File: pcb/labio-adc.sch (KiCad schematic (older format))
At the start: 14 parts, among them P301 CONN_01X04, P302 CONN_01X04, P303 CONN_01X04, Q301 PHOTOTRANSISTOR, Q302 Q_NMOS_GSD, Q303 Q_NMOS_GSD, SW301 DIP_SWITCH_X04, U301 ADS1015

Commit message: finish rerouting for new parts
* fix adc power supply nets
* redo adc layout
* move motor controller up to make space for headers
* add motor controller heatsink mount
* fix motor controller ground pad net

todo:
* silkscreen
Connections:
- net VDD_J is gone; now on net VDD5V_J: R301.1
- net SCL_5V: now reaches Q302.3 (D), R303.2, U301.10 (SCL)
- net SDA_5V: now reaches Q303.3 (D), R304.2, U301.9 (SDA)
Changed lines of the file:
@@
 $Descr A4 11693 8268
 encoding utf-8
-Sheet 3 9
+Sheet 3 10
 Title ""
 Date ""
@@
 INT_J
 Text Label 5100 4600 0    60   ~ 0
-VDD_J
+VDD5V_J
 $Comp
 L Q_NMOS_GSD Q303
@@
 Text Notes 7100 6000 0    60   ~ 0
 5V <=> 3.3V level shifting
+Text Label 7000 4700 0    60   ~ 0
+SDA_5V
+Text Label 7000 5400 0    60   ~ 0
+SCL_5V
 $EndSCHEMATC

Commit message: add bom. change led resistors to 220 and dnp rpi hat eeprom
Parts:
- R302: value 2k -> 220
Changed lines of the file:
@@
 P 8100 3800
 F 0 "R302" H 8130 3820 50  0000 L CNN
-F 1 "2k" H 8130 3760 50  0000 L CNN
+F 1 "220" H 8130 3760 50  0000 L CNN
 F 2 "Resistors_SMD:R_0603" H 8100 3800 50  0001 C CNN
 F 3 "" H 8100 3800 50  0000 C CNN

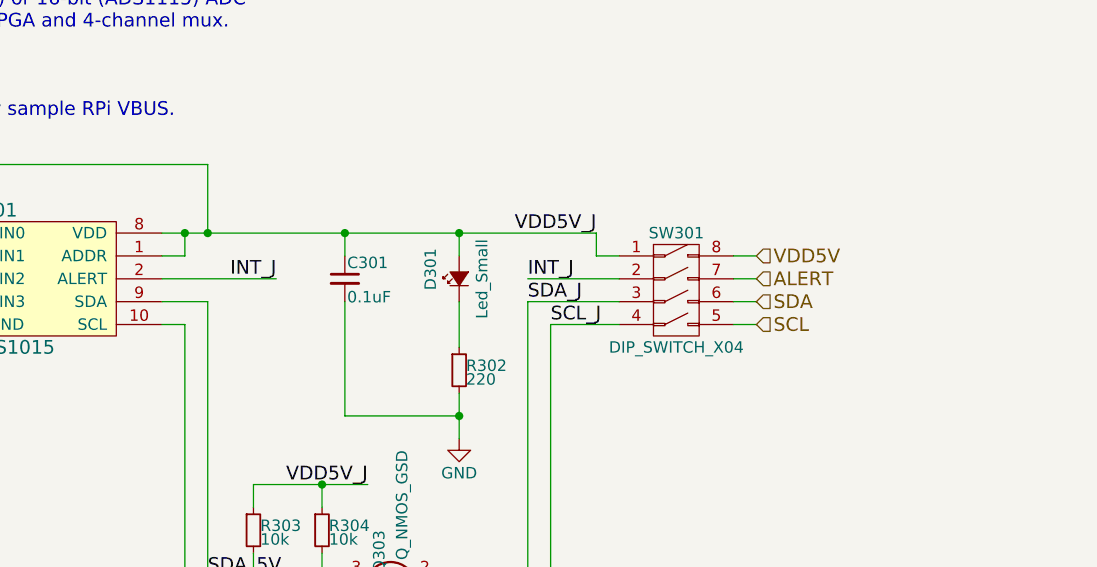
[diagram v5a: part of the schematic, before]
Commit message: add fuses for connectable headers (adc, encoder, motors, servo, codec). GERBER/BOM UPDATES ONLY
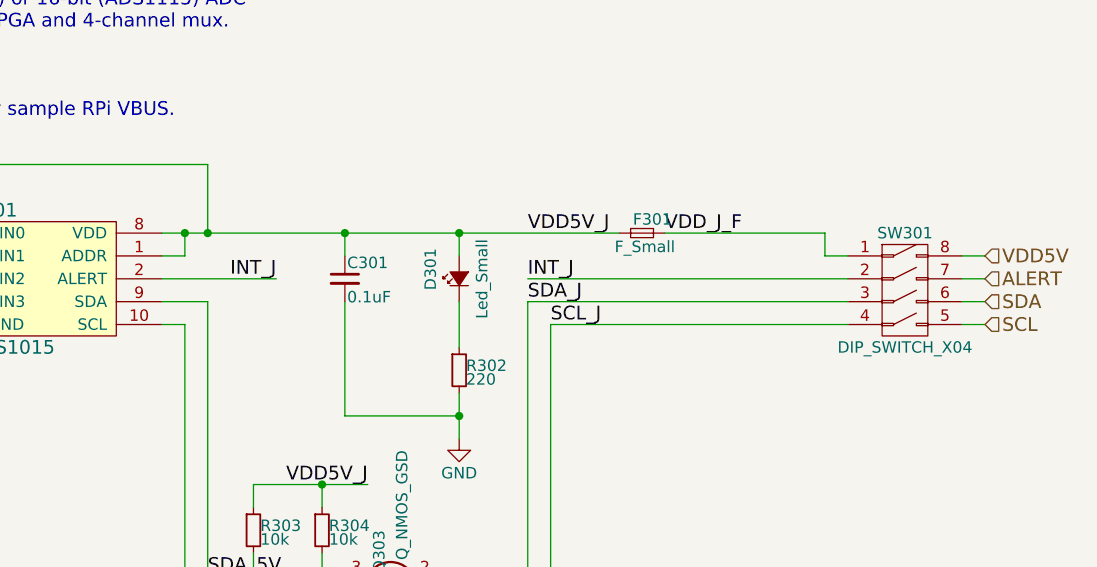
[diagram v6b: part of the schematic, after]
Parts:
- added F301: F_Small, Resistors_SMD:R_1206, symbol F_Small
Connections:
- net VDD5V_J: now also F301.1; no longer SW301.1 (1A)
- new net VDD_J_F: F301.2, SW301.1 (1A)
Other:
- moved on the sheet: SW301
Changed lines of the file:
@@
 	1    0    0    -1
 $EndComp
-Text HLabel 9400 3300 2    60   Input ~ 0
+Text HLabel 10400 3300 2    60   Input ~ 0
 VDD5V
-Text HLabel 9400 3500 2    60   Input ~ 0
+Text HLabel 10400 3500 2    60   Input ~ 0
 SDA
-Text HLabel 9400 3600 2    60   Input ~ 0
+Text HLabel 10400 3600 2    60   Input ~ 0
 SCL
-Text HLabel 9400 3400 2    60   Input ~ 0
+Text HLabel 10400 3400 2    60   Input ~ 0
 ALERT
 Wire Wire Line
@@
 L DIP_SWITCH_X04 SW301
 U 1 1 576D562D
-P 9050 3450
-F 0 "SW301" H 9050 3700 50  0000 C CNN
-F 1 "DIP_SWITCH_X04" H 9050 3200 50  0000 C CNN
-F 2 "labio-special:DIP-8_W7.62mm_SMT" H 9050 2250 50  0001 C CNN
-F 3 "" H 9050 2250 50  0000 C CNN
-	1    9050 3450
+P 10050 3450
+F 0 "SW301" H 10050 3700 50  0000 C CNN
+F 1 "DIP_SWITCH_X04" H 10050 3200 50  0000 C CNN
+F 2 "labio-special:DIP-8_W7.62mm_SMT" H 10050 2250 50  0001 C CNN
+F 3 "" H 10050 2250 50  0000 C CNN
+	1    10050 3450
 	1    0    0    -1
 $EndComp
@@
 	8100 3500 8100 3700
 Wire Wire Line
-	8800 3400 8400 3400
-Wire Wire Line
-	8400 3500 8800 3500
-Wire Wire Line
-	8800 3600 8500 3600
-Wire Wire Line
-	8800 3300 8700 3300
-Wire Wire Line
-	8700 3300 8700 3200
-Wire Wire Line
-	8700 3200 6800 3200
+	9800 3400 8400 3400
+Wire Wire Line
+	8400 3500 9800 3500
+Wire Wire Line
+	9800 3600 8500 3600
+Wire Wire Line
+	6800 3200 8800 3200
 Wire Wire Line
 	6900 3300 6900 3200
@@
 Connection ~ 8100 3200
 Wire Wire Line
-	9400 3300 9300 3300
-Wire Wire Line
-	9300 3400 9400 3400
-Wire Wire Line
-	9400 3500 9300 3500
-Wire Wire Line
-	9300 3600 9400 3600
-Text Label 8700 3200 2    60   ~ 0
+	10400 3300 10300 3300
+Wire Wire Line
+	10300 3400 10400 3400
+Wire Wire Line
+	10400 3500 10300 3500
+Wire Wire Line
+	10300 3600 10400 3600
+Text Label 8400 3200 0    60   ~ 0
 VDD5V_J
 Text Label 8400 3400 0    60   ~ 0
@@
 Text Label 7000 5400 0    60   ~ 0
 SCL_5V
+$Comp
+L F_Small F301
+U 1 1 57A54096
+P 8900 3200
+F 0 "F301" H 8860 3260 50  0000 L CNN
+F 1 "F_Small" H 8780 3140 50  0000 L CNN
+F 2 "Resistors_SMD:R_1206" H 8900 3200 50  0001 C CNN
+F 3 "" H 8900 3200 50  0000 C CNN
+	1    8900 3200
+	1    0    0    -1
+$EndComp
+Wire Wire Line
+	9000 3200 9700 3200
+Wire Wire Line
+	9700 3200 9700 3300
+Wire Wire Line
+	9700 3300 9800 3300
+Text Label 9000 3200 0    60   ~ 0
+VDD_J_F
 $EndSCHEMATC

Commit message: Fix ADC reading mic, possible backpowering, encoder pull downs, vias in footprint:
* Mic needs on-board path to ADC. Add proper bias and amp. Connect to ADC or codec with switches.
* Mic footprint (U701) flipped. Redraw footprint and adjust routing.
* Remove power from dip switches and replace with fuses. Turning power off to a block could result in backpower from driven IO lines.
* Remove/adjust pull downs on LEDs for encoder/dpad lines.
* Move vias out of display connector (P401) footprint.
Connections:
- net ADC_AIN2: now also SW301.1 (1A)
- net VDD5V: now also F301.2; no longer SW301.8 (1B)
- net ACD_AIN0 renamed ADC_AIN0
- removed net VDD_J_F: F301.2, SW301.1 (1A)
- new net MEMS_MIC_TO_ADC: SW301.8 (1B)
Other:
- moved on the sheet: F301, SW301
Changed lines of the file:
@@
 encoding utf-8
 Sheet 3 10
-Title ""
+Title "Raspberry Pi Embedded Lab I/O"
 Date ""
-Rev ""
-Comp ""
+Rev "1.1.4"
+Comp "Carnegie Mellon University"
 Comment1 ""
-Comment2 ""
+Comment2 "Drawn by: Ian Hartwig"
 Comment3 ""
 Comment4 ""
@@
 	1    0    0    -1
 $EndComp
-Text HLabel 10400 3300 2    60   Input ~ 0
+Text HLabel 9500 3000 2    60   Input ~ 0
 VDD5V
-Text HLabel 10400 3500 2    60   Input ~ 0
+Text HLabel 10100 3500 2    60   Input ~ 0
 SDA
-Text HLabel 10400 3600 2    60   Input ~ 0
+Text HLabel 10100 3600 2    60   Input ~ 0
 SCL
-Text HLabel 10400 3400 2    60   Input ~ 0
+Text HLabel 10100 3400 2    60   Input ~ 0
 ALERT
 Wire Wire Line
@@
 12-bit (ADS1015) or 16-bit (ADS1115) ADC\nwith differential PGA and 4-channel mux.\n\n7-bit addr: 0x73\n\n5V VDD to safely sample RPi VBUS.
 Text Label 5300 3200 0    60   ~ 0
-ACD_AIN0
+ADC_AIN0
 Text Label 5300 3300 0    60   ~ 0
 ADC_AIN1
@@
 L DIP_SWITCH_X04 SW301
 U 1 1 576D562D
-P 10050 3450
-F 0 "SW301" H 10050 3700 50  0000 C CNN
-F 1 "DIP_SWITCH_X04" H 10050 3200 50  0000 C CNN
-F 2 "labio-special:DIP-8_W7.62mm_SMT" H 10050 2250 50  0001 C CNN
-F 3 "" H 10050 2250 50  0000 C CNN
-	1    10050 3450
+P 9750 3450
+F 0 "SW301" H 9750 3700 50  0000 C CNN
+F 1 "DIP_SWITCH_X04" H 9750 3200 50  0000 C CNN
+F 2 "labio-special:DIP-8_W7.62mm_SMT" H 9750 2250 50  0001 C CNN
+F 3 "" H 9750 2250 50  0000 C CNN
+	1    9750 3450
 	1    0    0    -1
 $EndComp
@@
 	8100 3500 8100 3700
 Wire Wire Line
-	9800 3400 8400 3400
-Wire Wire Line
-	8400 3500 9800 3500
-Wire Wire Line
-	9800 3600 8500 3600
-Wire Wire Line
-	6800 3200 8800 3200
+	9500 3400 8400 3400
+Wire Wire Line
+	8400 3500 9500 3500
+Wire Wire Line
+	9500 3600 8500 3600
+Wire Wire Line
+	6800 3200 8400 3200
 Wire Wire Line
 	6900 3300 6900 3200
@@
 Connection ~ 7600 3200
 Wire Wire Line
-	8100 3300 8100 3200
+	8100 3200 8100 3300
 Connection ~ 8100 3200
 Wire Wire Line
-	10400 3300 10300 3300
-Wire Wire Line
-	10300 3400 10400 3400
-Wire Wire Line
-	10400 3500 10300 3500
-Wire Wire Line
-	10300 3600 10400 3600
-Text Label 8400 3200 0    60   ~ 0
+	10100 3300 10000 3300
+Wire Wire Line
+	10000 3400 10100 3400
+Wire Wire Line
+	10100 3500 10000 3500
+Wire Wire Line
+	10000 3600 10100 3600
+Text Label 8400 3000 0    60   ~ 0
 VDD5V_J
 Text Label 8400 3400 0    60   ~ 0
@@
 L F_Small F301
 U 1 1 57A54096
-P 8900 3200
-F 0 "F301" H 8860 3260 50  0000 L CNN
-F 1 "F_Small" H 8780 3140 50  0000 L CNN
-F 2 "Resistors_SMD:R_1206" H 8900 3200 50  0001 C CNN
-F 3 "" H 8900 3200 50  0000 C CNN
-	1    8900 3200
-	1    0    0    -1
-$EndComp
-Wire Wire Line
-	9000 3200 9700 3200
-Wire Wire Line
-	9700 3200 9700 3300
-Wire Wire Line
-	9700 3300 9800 3300
-Text Label 9000 3200 0    60   ~ 0
+P 8900 3000
+F 0 "F301" H 8860 3060 50  0000 L CNN
+F 1 "F_Small" H 8780 2940 50  0000 L CNN
+F 2 "Resistors_SMD:R_1206" H 8900 3000 50  0001 C CNN
+F 3 "" H 8900 3000 50  0000 C CNN
+	1    8900 3000
+	1    0    0    -1
+$EndComp
+Text Label 9100 3000 0    60   ~ 0
 VDD_J_F
+Text GLabel 10100 3300 2    60   Input ~ 0
+MEMS_MIC_TO_ADC
+Wire Wire Line
+	9500 3300 8800 3300
+Text Label 8800 3300 0    60   ~ 0
+ADC_AIN2
+Wire Wire Line
+	9000 3000 9500 3000
+Wire Wire Line
+	8800 3000 8400 3000
+Wire Wire Line
+	8400 3000 8400 3200
 $EndSCHEMATC

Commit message: Fix i2c addresses, pressure sensor footprint, consolidate BOM
* Schematic should list I2C addresses for accelerometer, gyro.
* Pressure sensor footprint (U502) has pins in the wrong order. Redraw footprint and adjust routing.
* Bump i2c and photodiode pullups to 2.2k
* Remove R505 near gyro
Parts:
- R301: value 1.5k -> 2.2k
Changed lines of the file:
@@
 P 5700 4800
 F 0 "R301" H 5730 4820 50  0000 L CNN
-F 1 "1.5k" H 5730 4760 50  0000 L CNN
+F 1 "2.2k" H 5730 4760 50  0000 L CNN
 F 2 "Resistors_SMD:R_0603" H 5700 4800 50  0001 C CNN
 F 3 "" H 5700 4800 50  0000 C CNN
